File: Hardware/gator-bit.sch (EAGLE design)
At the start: 89 parts, among them J1 GATOR, J10 GATOR, J11 GATOR, J12 GATOR, J13 GATOR, J14 GATOR, J15 GATOR, J16 GATOR, J17 GATOR, J18 GATOR, J2 GATOR, J3 GATOR, J4 GATOR, J6 GATOR, J7 GATOR, J8 GATOR, J9 GATOR, U1 TPS63070, U2 micro:bit, U3 V_REG_MIC52053.0V, U4 ADJ REG 1.5A

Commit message: Updates Per QC Review
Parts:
- renumbered 13 to D13
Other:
- note added: "Vin at Gator Tabs: 2.7V - 9V"
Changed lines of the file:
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@@
 <part name="C5" library="SparkFun-Capacitors" deviceset="0.1UF" device="-0603-25V-(+80/-20%)" value="0.1uF"/>
 <part name="GND19" library="SparkFun-PowerSymbols" deviceset="GND" device=""/>
-<part name="13" library="SparkFun-DiscreteSemi" deviceset="DIODE-ZENER" device="-MM3Z3V3T1G" value="3.3V"/>
+<part name="D13" library="SparkFun-DiscreteSemi" deviceset="DIODE-ZENER" device="-MM3Z3V3T1G" value="3.3V"/>
 <part name="R13" library="SparkFun-Resistors" deviceset="600OHM" device="" technology="OHMS-0603-1/10W-1%" value="604"/>
 <part name="GND22" library="SparkFun-PowerSymbols" deviceset="GND" device=""/>
@@
 <text x="101.6" y="35.56" size="5.08" layer="97" font="vector">Decoupling</text>
 <text x="154.94" y="43.18" size="5.08" layer="97" font="vector">IO Protection</text>
-<text x="200.914" y="158.496" size="1.778" layer="97">To use speaker Pin0
+<text x="200.914" y="158.496" size="1.27" layer="97" font="vector">To use speaker Pin0
 can not be used anymore</text>
-<text x="200.914" y="133.096" size="1.778" layer="97">Battery or external
+<text x="200.914" y="133.096" size="1.524" layer="97" font="vector">Battery or external
 supply</text>
-<text x="198.374" y="112.776" size="1.778" layer="97">Turn on regulated output</text>
+<text x="200.914" y="112.776" size="1.524" layer="97" font="vector">Turn on regulated
+ output</text>
+<text x="160.02" y="170.18" size="1.778" layer="97" font="vector">Vin at Gator Tabs:
+  2.7V - 9V</text>
 </plain>
 <instances>
@@
 <instance part="C5" gate="G$1" x="124.46" y="25.4" rot="R180"/>
 <instance part="GND19" gate="1" x="124.46" y="12.7"/>
-<instance part="13" gate="G$1" x="220.98" y="55.88" rot="R90"/>
+<instance part="D13" gate="G$1" x="220.98" y="55.88" rot="R90"/>
 <instance part="R13" gate="G$1" x="228.6" y="60.96" rot="R180"/>
 <instance part="GND22" gate="1" x="220.98" y="48.26"/>
@@
 <instance part="SUPPLY28" gate="G$1" x="73.66" y="121.92"/>
 <instance part="S2" gate="1" x="208.28" y="142.24"/>
-<instance part="SUPPLY29" gate="G$1" x="203.2" y="144.78"/>
-<instance part="D6" gate="G$1" x="218.44" y="144.78" rot="R180"/>
+<instance part="SUPPLY29" gate="G$1" x="203.2" y="144.78" smashed="yes">
+<attribute name="VALUE" x="203.2" y="147.574" size="1.778" layer="96" align="bottom-center"/>
+</instance>
+<instance part="D6" gate="G$1" x="218.44" y="144.78" smashed="yes" rot="R180">
+<attribute name="NAME" x="218.44" y="148.336" size="1.778" layer="95" font="vector" rot="R180"/>
+<attribute name="VALUE" x="231.14" y="149.352" size="1.778" layer="96" font="vector" rot="R180" align="top-left"/>
+</instance>
 </instances>
 <busses>
@@
 </segment>
 <segment>
-<pinref part="13" gate="G$1" pin="A"/>
+<pinref part="D13" gate="G$1" pin="A"/>
 <wire x1="220.98" y1="53.34" x2="220.98" y2="50.8" width="0.1524" layer="91"/>
 <pinref part="GND22" gate="1" pin="GND"/>
@@
 <wire x1="220.98" y1="60.96" x2="218.44" y2="60.96" width="0.1524" layer="91"/>
 <wire x1="218.44" y1="63.5" x2="218.44" y2="60.96" width="0.1524" layer="91"/>
-<pinref part="13" gate="G$1" pin="C"/>
+<pinref part="D13" gate="G$1" pin="C"/>
 <wire x1="220.98" y1="58.42" x2="220.98" y2="60.96" width="0.1524" layer="91"/>
 <junction x="220.98" y="60.96"/>
@@
 <wire x1="147.32" y1="35.56" x2="147.32" y2="88.9" width="0.1524" layer="97" style="longdash"/>
 <wire x1="78.74" y1="91.44" x2="78.74" y2="0" width="0.1524" layer="97" style="longdash"/>
-<text x="160.02" y="167.64" size="2.54" layer="97">5V Regulator
+<text x="160.02" y="167.64" size="2.54" layer="97" font="vector">5V Regulator
 2.7 - 9V
 Buck/Boost Switched</text>
-<text x="10.16" y="78.74" size="2.54" layer="97">3V Regulator
+<text x="10.16" y="78.74" size="2.54" layer="97" font="vector">3V Regulator
 5V input from TPS REG
 Powers Micro:bit only</text>
-<text x="81.28" y="78.74" size="2.54" layer="97">3.3V Regulator
+<text x="81.28" y="78.74" size="2.54" layer="97" font="vector">3.3V Regulator
 5V input from TPS REG
 Powers LEDs, 3.3V OUT</text>

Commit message: fixing 604 Resistor Package
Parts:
- R11, R13, R15, R17, R19, R7, R9: device SparkFun-Resistors:600OHMOHMS-0603-1/10W-1% -> SparkFun-Resistors:604OHMOHMS-0603-1/10W-1%
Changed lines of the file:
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@@
 <part name="GND19" library="SparkFun-PowerSymbols" deviceset="GND" device=""/>
 <part name="D13" library="SparkFun-DiscreteSemi" deviceset="DIODE-ZENER" device="-MM3Z3V3T1G" value="3.3V"/>
-<part name="R13" library="SparkFun-Resistors" deviceset="600OHM" device="" technology="OHMS-0603-1/10W-1%" value="604"/>
+<part name="R13" library="SparkFun-Resistors" deviceset="604OHM" device="" technology="OHMS-0603-1/10W-1%" value="604"/>
 <part name="GND22" library="SparkFun-PowerSymbols" deviceset="GND" device=""/>
 <part name="FRAME3" library="SparkFun-Aesthetics" deviceset="FRAME-LETTER" device=""/>
@@
 <part name="R6" library="SparkFun-Resistors" deviceset="910OHM" device="" technology="OHMS-0603-1/10W-1%" value="910"/>
 <part name="D8" library="SparkFun-DiscreteSemi" deviceset="DIODE-ZENER" device="-MM3Z3V3T1G" value="3.3V"/>
-<part name="R7" library="SparkFun-Resistors" deviceset="600OHM" device="" technology="OHMS-0603-1/10W-1%" value="604"/>
+<part name="R7" library="SparkFun-Resistors" deviceset="604OHM" device="" technology="OHMS-0603-1/10W-1%" value="604"/>
 <part name="GND2" library="SparkFun-PowerSymbols" deviceset="GND" device=""/>
 <part name="D9" library="SparkFun-DiscreteSemi" deviceset="DIODE-ZENER" device="-MM3Z3V3T1G" value="3.3V"/>
@@
 <part name="R8" library="SparkFun-Resistors" deviceset="910OHM" device="" technology="OHMS-0603-1/10W-1%" value="910"/>
 <part name="D10" library="SparkFun-DiscreteSemi" deviceset="DIODE-ZENER" device="-MM3Z3V3T1G" value="3.3V"/>
-<part name="R9" library="SparkFun-Resistors" deviceset="600OHM" device="" technology="OHMS-0603-1/10W-1%" value="604"/>
+<part name="R9" library="SparkFun-Resistors" deviceset="604OHM" device="" technology="OHMS-0603-1/10W-1%" value="604"/>
 <part name="GND12" library="SparkFun-PowerSymbols" deviceset="GND" device=""/>
 <part name="D11" library="SparkFun-DiscreteSemi" deviceset="DIODE-ZENER" device="-MM3Z3V3T1G" value="3.3V"/>
@@
 <part name="R10" library="SparkFun-Resistors" deviceset="910OHM" device="" technology="OHMS-0603-1/10W-1%" value="910"/>
 <part name="D12" library="SparkFun-DiscreteSemi" deviceset="DIODE-ZENER" device="-MM3Z3V3T1G" value="3.3V"/>
-<part name="R11" library="SparkFun-Resistors" deviceset="600OHM" device="" technology="OHMS-0603-1/10W-1%" value="604"/>
+<part name="R11" library="SparkFun-Resistors" deviceset="604OHM" device="" technology="OHMS-0603-1/10W-1%" value="604"/>
 <part name="GND13" library="SparkFun-PowerSymbols" deviceset="GND" device=""/>
 <part name="D14" library="SparkFun-DiscreteSemi" deviceset="DIODE-ZENER" device="-MM3Z3V3T1G" value="3.3V"/>
@@
 <part name="R14" library="SparkFun-Resistors" deviceset="910OHM" device="" technology="OHMS-0603-1/10W-1%" value="910"/>
 <part name="D15" library="SparkFun-DiscreteSemi" deviceset="DIODE-ZENER" device="-MM3Z3V3T1G" value="3.3V"/>
-<part name="R15" library="SparkFun-Resistors" deviceset="600OHM" device="" technology="OHMS-0603-1/10W-1%" value="604"/>
+<part name="R15" library="SparkFun-Resistors" deviceset="604OHM" device="" technology="OHMS-0603-1/10W-1%" value="604"/>
 <part name="GND14" library="SparkFun-PowerSymbols" deviceset="GND" device=""/>
 <part name="D16" library="SparkFun-DiscreteSemi" deviceset="DIODE-ZENER" device="-MM3Z3V3T1G" value="3.3V"/>
@@
 <part name="R16" library="SparkFun-Resistors" deviceset="910OHM" device="" technology="OHMS-0603-1/10W-1%" value="910"/>
 <part name="D17" library="SparkFun-DiscreteSemi" deviceset="DIODE-ZENER" device="-MM3Z3V3T1G" value="3.3V"/>
-<part name="R17" library="SparkFun-Resistors" deviceset="600OHM" device="" technology="OHMS-0603-1/10W-1%" value="604"/>
+<part name="R17" library="SparkFun-Resistors" deviceset="604OHM" device="" technology="OHMS-0603-1/10W-1%" value="604"/>
 <part name="GND15" library="SparkFun-PowerSymbols" deviceset="GND" device=""/>
 <part name="D18" library="SparkFun-DiscreteSemi" deviceset="DIODE-ZENER" device="-MM3Z3V3T1G" value="3.3V"/>
@@
 <part name="R18" library="SparkFun-Resistors" deviceset="910OHM" device="" technology="OHMS-0603-1/10W-1%" value="910"/>
 <part name="D19" library="SparkFun-DiscreteSemi" deviceset="DIODE-ZENER" device="-MM3Z3V3T1G" value="3.3V"/>
-<part name="R19" library="SparkFun-Resistors" deviceset="600OHM" device="" technology="OHMS-0603-1/10W-1%" value="604"/>
+<part name="R19" library="SparkFun-Resistors" deviceset="604OHM" device="" technology="OHMS-0603-1/10W-1%" value="604"/>
 <part name="GND16" library="SparkFun-PowerSymbols" deviceset="GND" device=""/>
 <part name="D20" library="SparkFun-DiscreteSemi" deviceset="DIODE-ZENER" device="-MM3Z3V3T1G" value="3.3V"/>

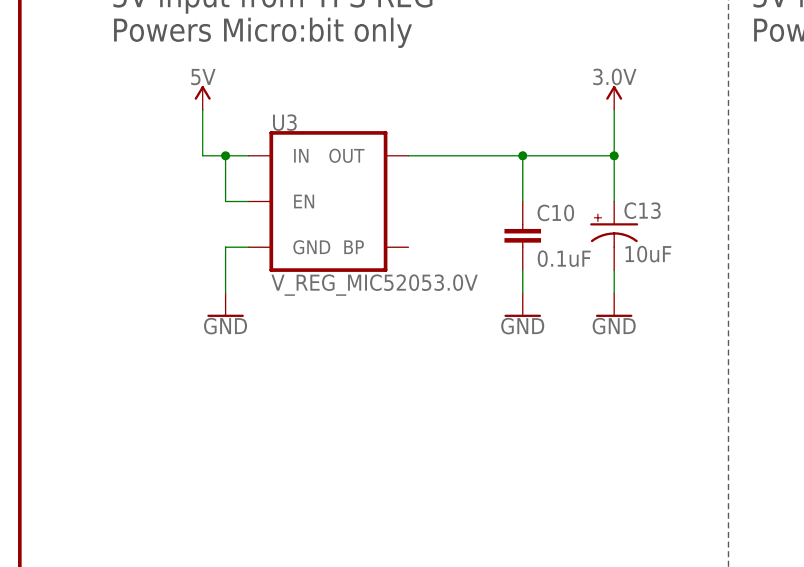
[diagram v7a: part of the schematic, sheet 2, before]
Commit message: Updating VREG 3.0V Package
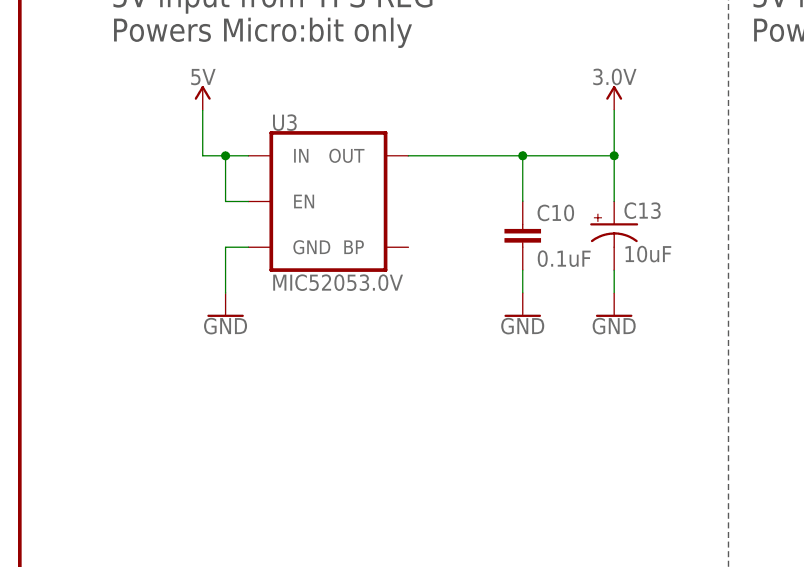
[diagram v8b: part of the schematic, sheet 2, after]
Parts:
- U3: value V_REG_MIC52053.0V -> MIC52053.0V
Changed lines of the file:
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@@
 <part name="GND18" library="SparkFun-PowerSymbols" deviceset="GND" device=""/>
 <part name="GND20" library="SparkFun-PowerSymbols" deviceset="GND" device=""/>
-<part name="U3" library="SparkFun-IC-Power" deviceset="V_REG_MIC5205" device="3.0V"/>
+<part name="U3" library="SparkFun-IC-Power" deviceset="V_REG_MIC5205" device="3.0V" value="MIC52053.0V"/>
 <part name="SUPPLY20" library="SparkFun-PowerSymbols" deviceset="5V" device=""/>
 <part name="SUPPLY21" library="SparkFun-PowerSymbols" deviceset="5V" device=""/>
